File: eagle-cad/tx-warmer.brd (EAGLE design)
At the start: 44.5 x 44.5 mm, 21 parts

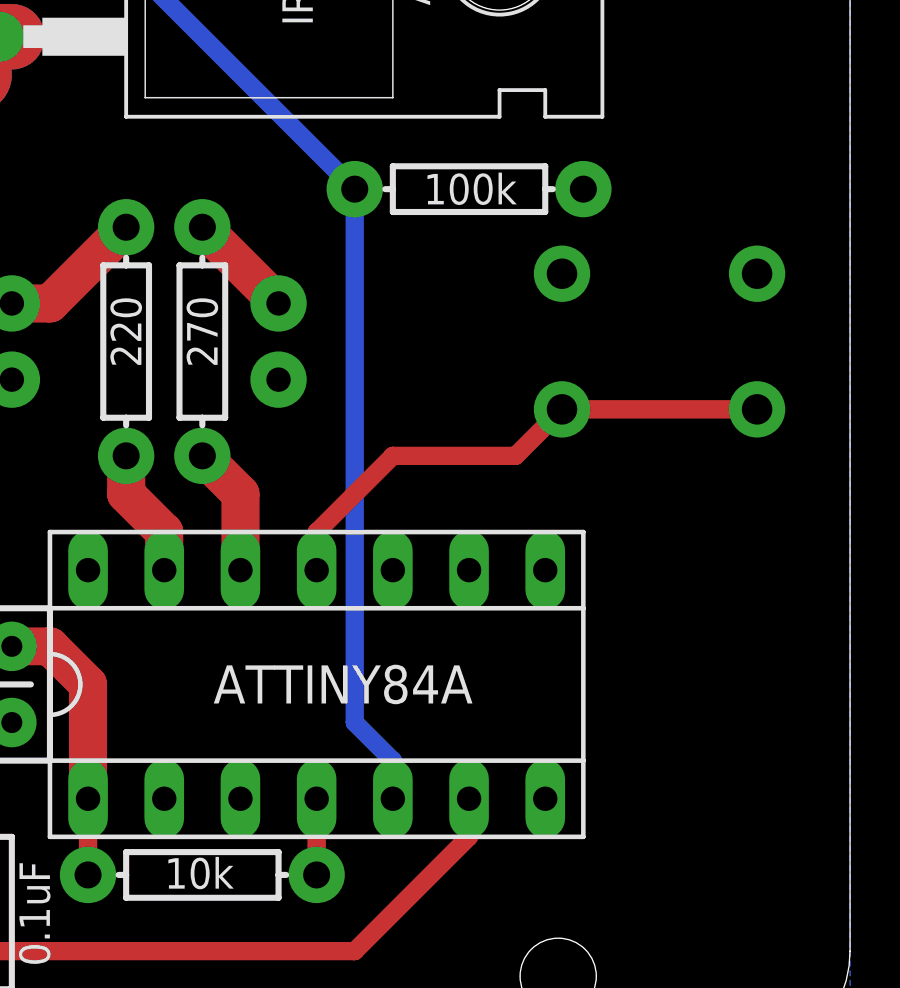
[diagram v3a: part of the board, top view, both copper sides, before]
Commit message: Moved PWM from pin5 to pin8
Reason for this to utilizer timer1 and allows using prescaler without
interference to delay-methods.
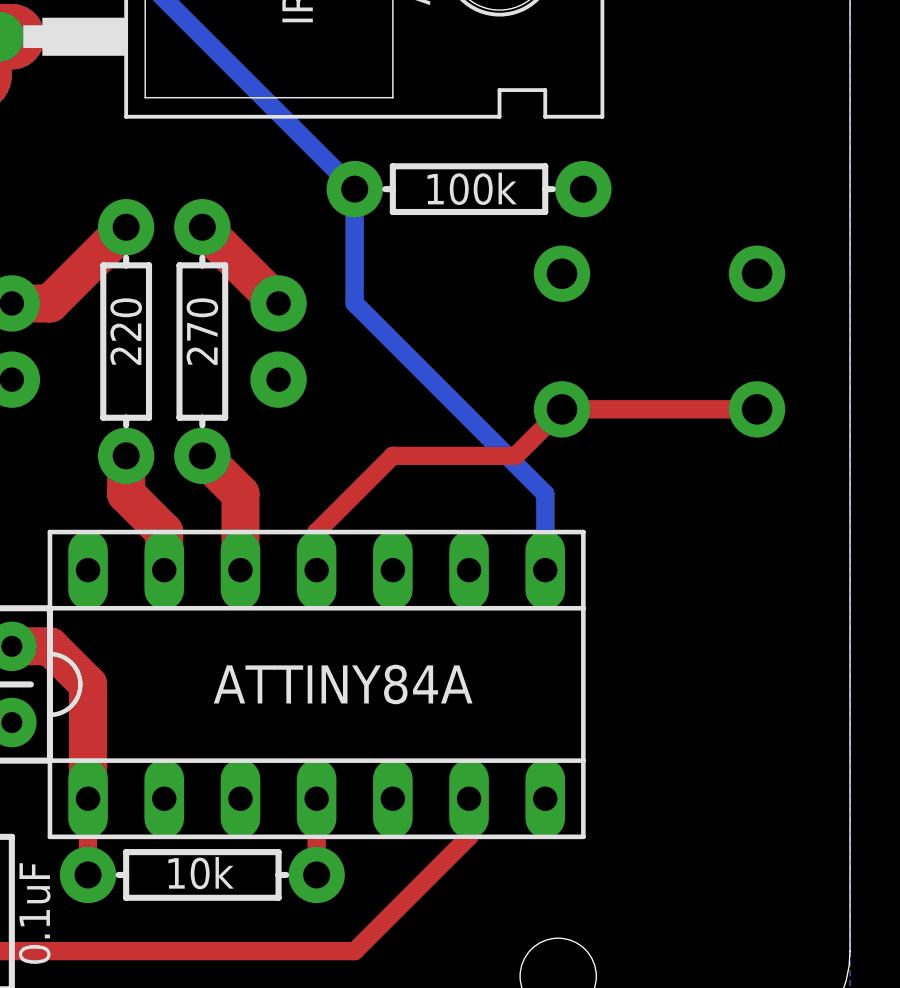
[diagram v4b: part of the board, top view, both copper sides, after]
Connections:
- net N$6: now also ATTINY84A.8; no longer ATTINY84A.5
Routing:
- net N$6: track 37.8 -> 32.2 mm
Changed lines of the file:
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@@
 <signal name="N$6">
 <contactref element="IRLB8743" pad="1"/>
-<contactref element="ATTINY84A" pad="5"/>
 <contactref element="R6" pad="P$1"/>
 <wire x1="13.97" y1="38.1" x2="16.51" y2="38.1" width="0.6096" layer="16"/>
 <wire x1="16.51" y1="38.1" x2="26.67" y2="27.94" width="0.6096" layer="16"/>
-<wire x1="27.94" y1="7.62" x2="27.94" y2="8.89" width="0.6096" layer="16"/>
-<wire x1="27.94" y1="8.89" x2="26.67" y2="10.16" width="0.6096" layer="16"/>
-<wire x1="26.67" y1="10.16" x2="26.67" y2="27.94" width="0.6096" layer="16"/>
+<contactref element="ATTINY84A" pad="8"/>
+<wire x1="33.02" y1="15.24" x2="33.02" y2="17.78" width="0.6096" layer="16"/>
+<wire x1="33.02" y1="17.78" x2="26.67" y2="24.13" width="0.6096" layer="16"/>
+<wire x1="26.67" y1="24.13" x2="26.67" y2="27.94" width="0.6096" layer="16"/>
 </signal>
 <signal name="N$7">

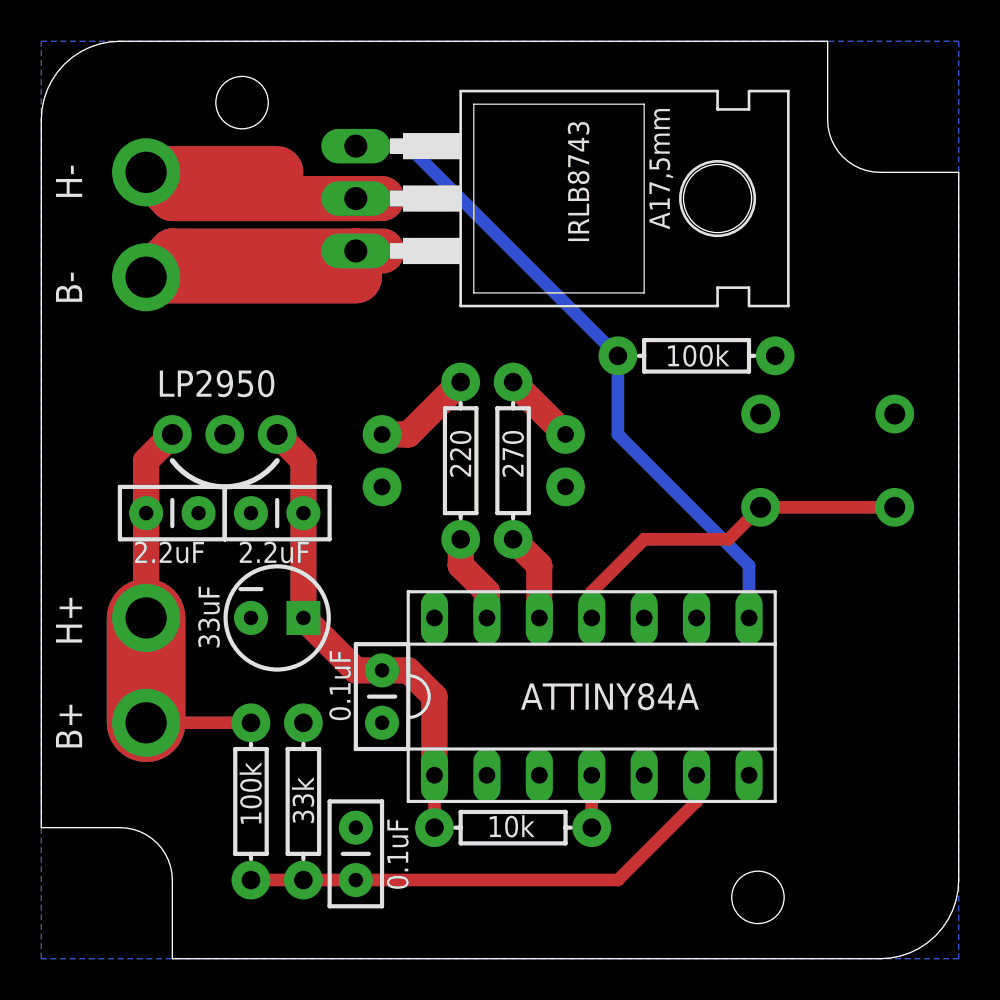
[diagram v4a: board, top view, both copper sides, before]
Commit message: Added DIP switches and refactored layout
Switches allow to configure software and reduces firmware variations.
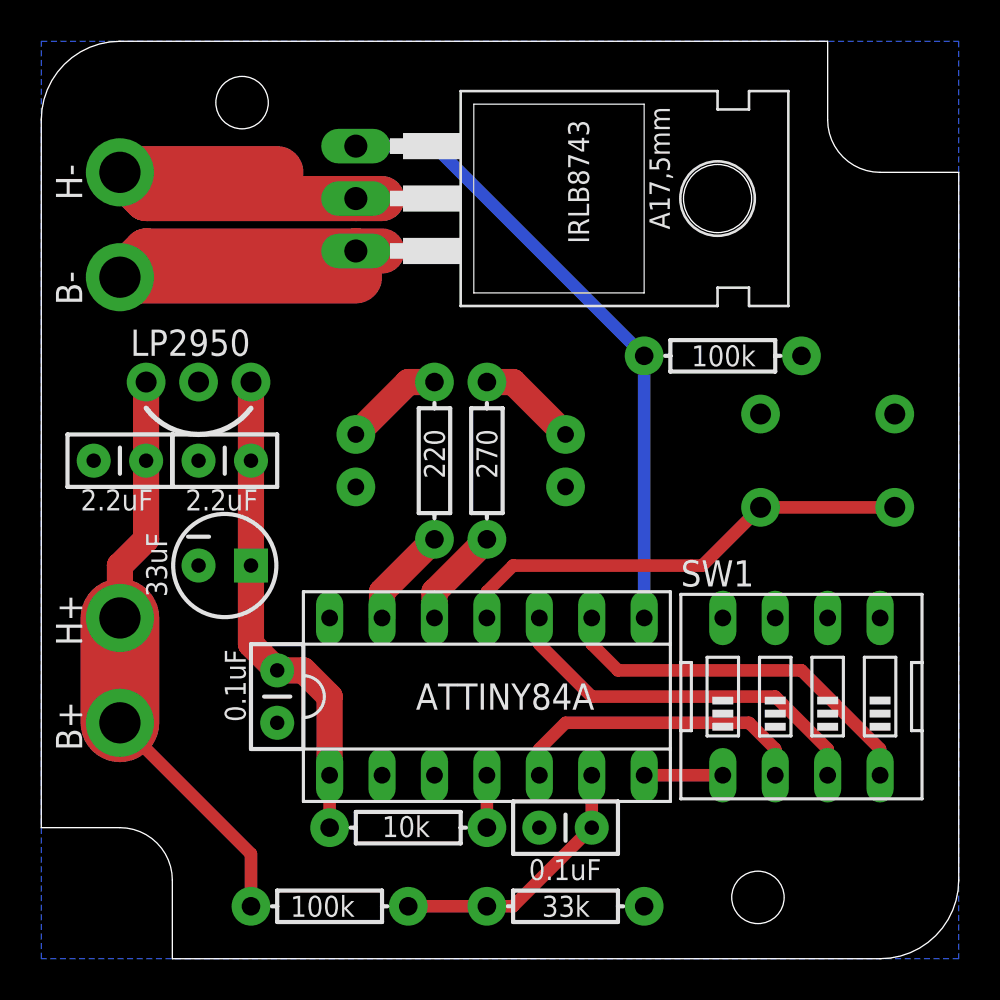
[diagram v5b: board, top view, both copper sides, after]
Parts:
- added SW1: (no value), special:EDG-04
- moved R4 13.7 mm to (24.1, 1.27), turned to 0 degrees
- moved C6 11.7 mm to (25.4, 5.08), turned to 180 degrees
- moved R3 6.35 mm to (12.7, 1.27), turned to 0 degrees
- moved C3 5.08 mm to (10.2, 12.7)
- moved ATTINY84A 5.08 mm to (20.3, 11.4)
- moved R1 5.08 mm to (16.5, 5.08)
- moved C5 3.59 mm to (7.62, 17.8)
- moved C1 3.59 mm to (8.89, 22.9)
- moved LP2950 2.84 mm to (3.81, 26.7)
- moved C2 2.54 mm to (3.81, 22.9), turned to 180 degrees
- moved B+ 1.27 mm to (2.54, 10.2)
- moved B- 1.27 mm to (2.54, 31.8)
- moved H+ 1.27 mm to (2.54, 15.2)
- moved H- 1.27 mm to (2.54, 36.8)
- moved LED1 1.27 mm to (14.0, 22.9)
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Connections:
- new net N$1: ATTINY84A.7, SW1.1
- new net N$2: ATTINY84A.5, SW1.2
- new net N$20: ATTINY84A.9, SW1.4
- new net N$5: ATTINY84A.10, SW1.3
- net GND: now also SW1.5, SW1.6, SW1.7, SW1.8
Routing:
- net N$5: track 0.00 -> 18.6 mm
- net N$20: track 0.00 -> 18.6 mm
- net N$2: track 0.00 -> 15.0 mm
- net N$7: track 24.4 -> 13.0 mm
- net N$4: track 24.7 -> 33.6 mm
- net N$13: track 17.6 -> 22.7 mm
- net N$19: track 36.6 -> 41.7 mm
- net GND: track 44.2 -> 49.3 mm
- net N$1: track 0.00 -> 3.81 mm
- net N$6: track 32.2 -> 30.9 mm
- net N$8: track 3.59 -> 4.86 mm
- net N$18: track 4.34 -> 4.86 mm
- net N$12: track 4.34 -> 4.86 mm
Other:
- board text added: "Pertti Erkkilä 2013"
- board text added: "TX-warmer v1.6"
- board text removed: "Pertti Erkkilä 2012"
- board text removed: "TX-warmer v1.5"
